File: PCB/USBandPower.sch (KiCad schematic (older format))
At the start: 16 parts

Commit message: WIP
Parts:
- added C?: 22uF, Capacitor_SMD:CP_Elec_10x10.5, symbol Device:CP
- added C?: 0.47uF, Capacitor_SMD:C_0805_2012Metric, symbol Device:C
- added U?: LM2940, Package_TO_SOT_SMD:SOT-223, symbol BritishIdeas:LM2940
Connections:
- net +12V: now also C?.1, U?.1 (IN)
- net GND: now also C?.2, C?.2, U?.2 (GND), U?.4 (GND)
- new net +10V: C?.1, U?.3 (OUT)
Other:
- moved on the sheet: C?, D?, L?, R?, U?

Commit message: WIP.
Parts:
- C?: value 4.7uF 16V e -> 4.7uF; symbol Device:CP -> Device:C
- D?: footprint LED_SMD:LED_PLCC-2 -> LED_SMD:LED_0603_1608Metric
- R?: value 1K -> 620
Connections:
- net +3V3: now also D?.2 (A)
- net +5V: no longer D?.2 (A)
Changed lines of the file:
@@
 $EndComp
 $Comp
-L Device:CP C?
+L Device:C C?
 U 1 1 604917D2
 P 9150 3750
 AR Path="/604917D2" Ref="C?"  Part="1"
 AR Path="/60479334/604917D2" Ref="C?"  Part="1"
-F 0 "C?" H 9250 3750 50  0000 L CNN
-F 1 "4.7uF 16V e" V 9000 3550 50  0000 L CNN
+F 0 "C?" H 8900 3800 50  0000 L CNN
+F 1 "4.7uF" H 8800 3700 50  0000 L CNN
 F 2 "Capacitor_SMD:CP_Elec_4x5.8" H 9188 3600 50  0001 C CNN
 F 3 "~" H 9150 3750 50  0001 C CNN
@@
 F 0 "D?" V 7589 2582 50  0000 R CNN
 F 1 "PWR" V 7498 2582 50  0000 R CNN
-F 2 "LED_SMD:LED_PLCC-2" H 7550 2700 50  0001 C CNN
+F 2 "LED_SMD:LED_0603_1608Metric" H 7550 2700 50  0001 C CNN
 F 3 "~" H 7550 2700 50  0001 C CNN
 	1    7550 2700
@@
 AR Path="/60479334/6045614D" Ref="R?"  Part="1"
 F 0 "R?" V 7343 3250 50  0000 C CNN
-F 1 "1K" V 7434 3250 50  0000 C CNN
+F 1 "620" V 7434 3250 50  0000 C CNN
 F 2 "Resistor_SMD:R_0805_2012Metric" V 7480 3250 50  0001 C CNN
 F 3 "~" H 7550 3250 50  0001 C CNN
 	1    7550 3250
 	-1   0    0    1
-$EndComp
-$Comp
-L power:+5V #PWR?
-U 1 1 60456153
-P 7550 2550
-F 0 "#PWR?" H 7550 2400 50  0001 C CNN
-F 1 "+5V" H 7565 2723 50  0000 C CNN
-F 2 "" H 7550 2550 50  0001 C CNN
-F 3 "" H 7550 2550 50  0001 C CNN
-	1    7550 2550
-	1    0    0    -1
 $EndComp
 $Comp
@@
 	8000 5300 8000 5450
 Connection ~ 8000 5450
+$Comp
+L power:+3V3 #PWR?
+U 1 1 61B0845B
+P 7550 2400
+AR Path="/61B0845B" Ref="#PWR?"  Part="1"
+AR Path="/60479334/61B0845B" Ref="#PWR?"  Part="1"
+F 0 "#PWR?" H 7550 2250 50  0001 C CNN
+F 1 "+3V3" H 7565 2573 50  0000 C CNN
+F 2 "" H 7550 2400 50  0001 C CNN
+F 3 "" H 7550 2400 50  0001 C CNN
+	1    7550 2400
+	1    0    0    -1
+$EndComp
+Wire Wire Line
+	7550 2400 7550 2550
 $EndSCHEMATC

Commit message: WIP
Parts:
- added J?: 12V IN, Britishideas:PhoenixContact_COMBICON_MKDSN_2, symbol Connector:Screw_Terminal_01x02
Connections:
- net +12V: now also J?.2 (Pin_2)
- net GND: now also J?.1 (Pin_1)
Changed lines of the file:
@@
 $Descr A4 11693 8268
 encoding utf-8
-Sheet 2 6
+Sheet 2 3
 Title "MPS Tune-o-Matic"
-Date "2021-12-06"
+Date "2022-02-19"
 Rev "V1.0"
-Comp "(C) andy@britishideas.com 2021"
+Comp "(C) andy@britishideas.com 2022"
 Comment1 "For Bosch D-Jetronic MPS Type 3"
 Comment2 ""
@@
 Wire Wire Line
 	7550 2400 7550 2550
+$Comp
+L power:+12V #PWR?
+U 1 1 62339678
+P 1750 5350
+AR Path="/62339678" Ref="#PWR?"  Part="1"
+AR Path="/60479334/62339678" Ref="#PWR?"  Part="1"
+F 0 "#PWR?" H 1750 5200 50  0001 C CNN
+F 1 "+12V" H 1765 5523 50  0000 C CNN
+F 2 "" H 1750 5350 50  0001 C CNN
+F 3 "" H 1750 5350 50  0001 C CNN
+	1    1750 5350
+	-1   0    0    -1
+$EndComp
+$Comp
+L power:PWR_FLAG #FLG?
+U 1 1 6233967E
+P 1750 5400
+AR Path="/6233967E" Ref="#FLG?"  Part="1"
+AR Path="/60479334/6233967E" Ref="#FLG?"  Part="1"
+F 0 "#FLG?" H 1750 5475 50  0001 C CNN
+F 1 "PWR_FLAG" V 1750 5528 50  0000 L CNN
+F 2 "" H 1750 5400 50  0001 C CNN
+F 3 "~" H 1750 5400 50  0001 C CNN
+	1    1750 5400
+	0    1    -1   0
+$EndComp
+Wire Wire Line
+	1750 5400 1750 5350
+$Comp
+L Connector:Screw_Terminal_01x02 J?
+U 1 1 62339686
+P 1500 5700
+AR Path="/62339686" Ref="J?"  Part="1"
+AR Path="/60479334/62339686" Ref="J?"  Part="1"
+F 0 "J?" H 1580 5692 50  0000 L CNN
+F 1 "12V IN" H 1580 5601 50  0000 L CNN
+F 2 "Britishideas:PhoenixContact_COMBICON_MKDSN_2" H 1500 5700 50  0001 C CNN
+F 3 "~" H 1500 5700 50  0001 C CNN
+F 4 "1729018" H 1500 5700 50  0001 C CNN "manf#"
+	1    1500 5700
+	-1   0    0    1
+$EndComp
+$Comp
+L power:GND #PWR?
+U 1 1 6233968C
+P 1750 5900
+AR Path="/6233968C" Ref="#PWR?"  Part="1"
+AR Path="/60479334/6233968C" Ref="#PWR?"  Part="1"
+F 0 "#PWR?" H 1750 5650 50  0001 C CNN
+F 1 "GND" H 1755 5727 50  0000 C CNN
+F 2 "" H 1750 5900 50  0001 C CNN
+F 3 "" H 1750 5900 50  0001 C CNN
+	1    1750 5900
+	-1   0    0    -1
+$EndComp
+Wire Wire Line
+	1750 5900 1750 5700
+Wire Wire Line
+	1750 5700 1700 5700
+Wire Wire Line
+	1700 5600 1750 5600
+Wire Wire Line
+	1750 5600 1750 5400
+Connection ~ 1750 5400
 $EndSCHEMATC

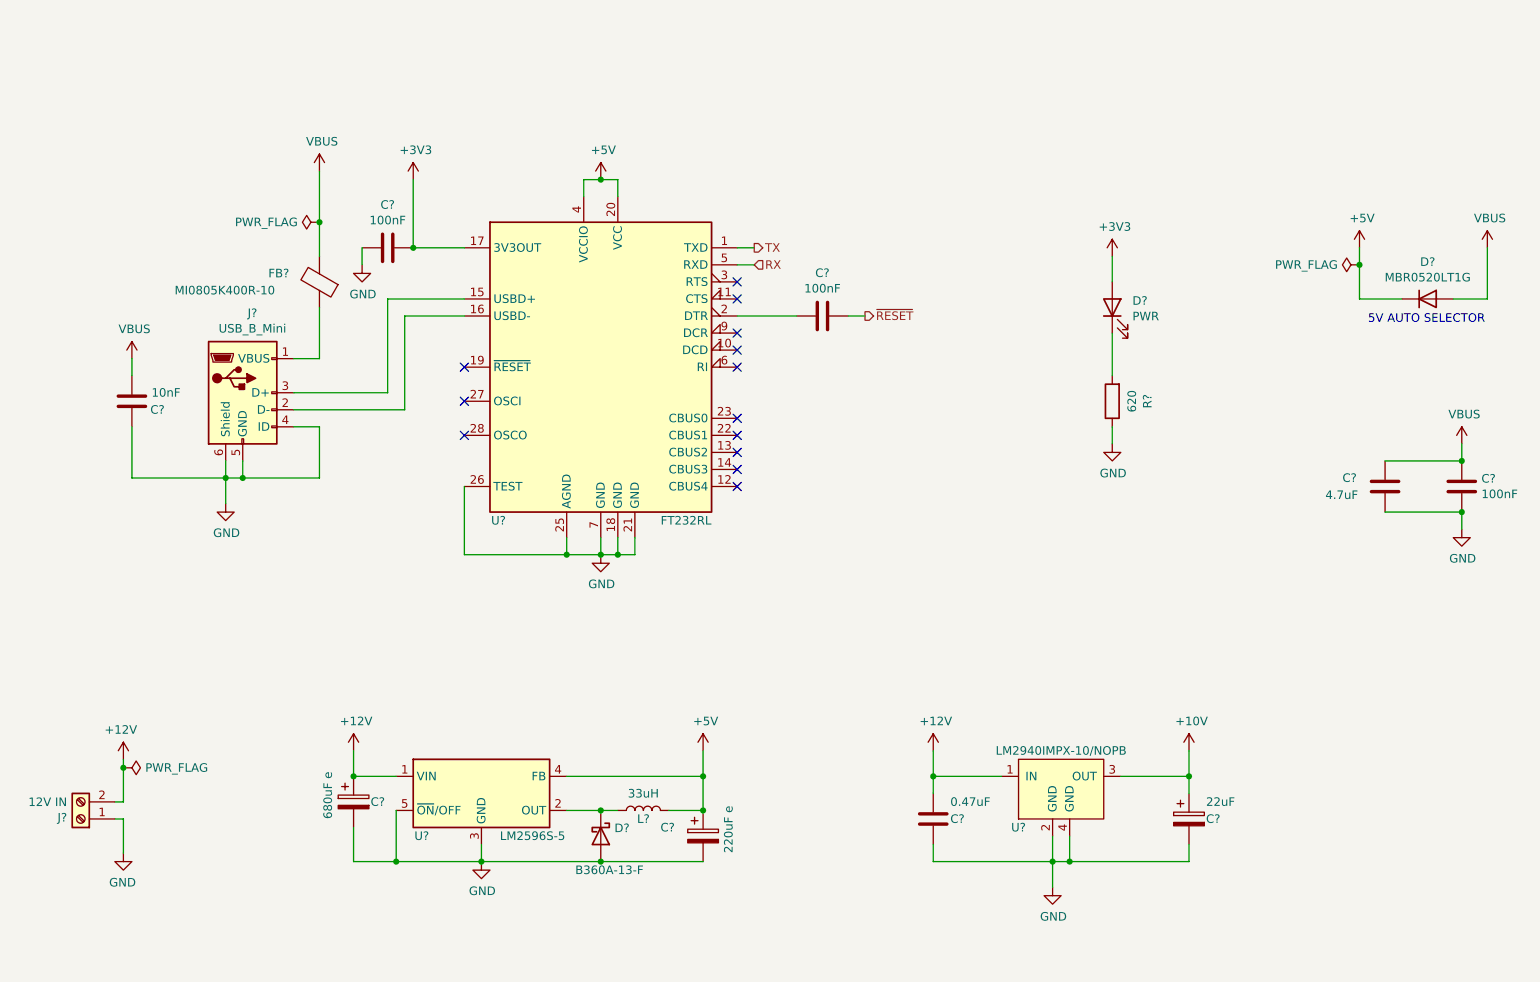
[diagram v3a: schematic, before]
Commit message: Completed schematic. Started work on PCB.
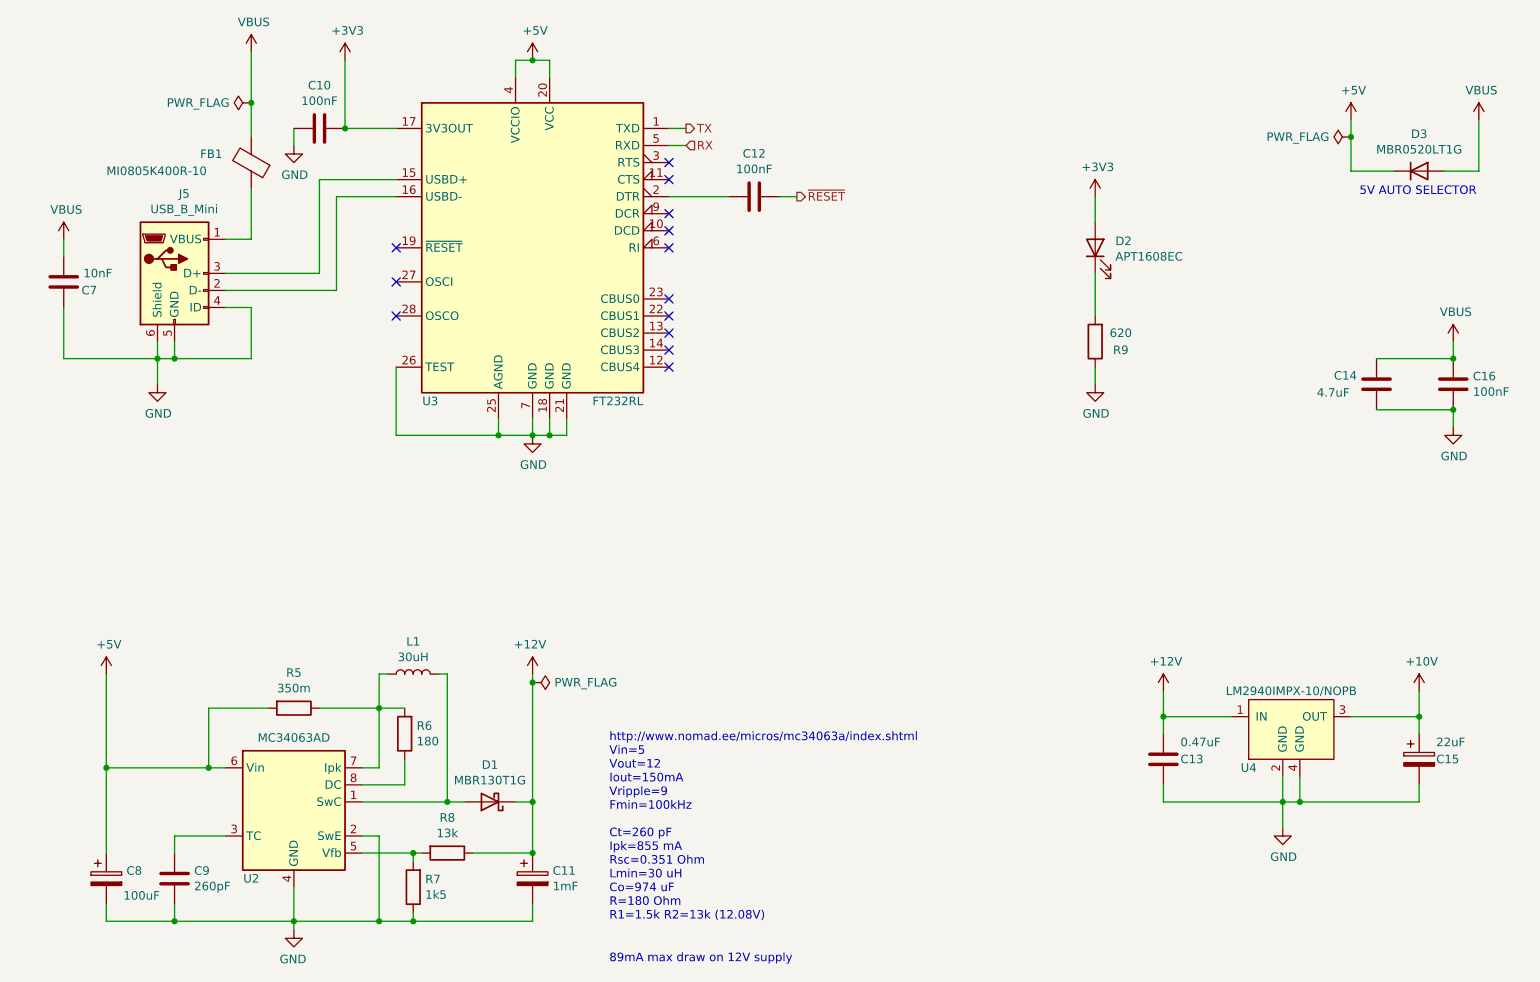
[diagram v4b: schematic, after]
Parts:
- removed C?: 680uF e, Capacitor_SMD:CP_Elec_10x10.5, symbol Device:CP
- removed C?: 220uF e, Capacitor_SMD:CP_Elec_8x6.5, symbol Device:CP
- removed D?: B360A-13-F, Diode_SMD:D_SMA, symbol Device:D_Schottky
- removed J?: 12V IN, Britishideas:PhoenixContact_COMBICON_MKDSN_2, symbol Connector:Screw_Terminal_01x02
- removed L?: 33uH, Britishideas:Wurth-WE-LQS-Inductor, symbol Device:L
- removed U?: LM2596S-5, Package_TO_SOT_SMD:TO-263-5_TabPin3, symbol Regulator_Switching:LM2596S-5
- added C11: 1mF, Capacitor_SMD:CP_Elec_10x10, symbol Device:CP
- added C8: 100uF, Capacitor_SMD:CP_Elec_6.3x5.3, symbol Device:CP
- added C9: 260pF, Capacitor_SMD:C_0603_1608Metric, symbol Device:C
- added D1: MBR130T1G, Britishideas:SOD-123, symbol Device:D_Schottky
- added L1: 30uH, Britishideas:Abracon ASPI-6045S Series Inductors, symbol Device:L
- added R5: 350m, Resistor_SMD:R_2010_5025Metric, symbol Device:R
- added R6: 180, Resistor_SMD:R_0603_1608Metric, symbol Device:R
- added R7: 1k5, Resistor_SMD:R_0603_1608Metric, symbol Device:R
- added R8: 13k, Resistor_SMD:R_0603_1608Metric, symbol Device:R
- added U2: MC34063AD, Package_SO:SOIC-8_3.9x4.9mm_P1.27mm, symbol Regulator_Switching:MC34063AD
- C10, C12, C13, C16, C7: renamed from C?; footprint Capacitor_SMD:C_0805_2012Metric -> Capacitor_SMD:C_0603_1608Metric
- D2: renamed from D?; value PWR -> APT1608EC; manf# (none) -> APT1608EC
- R9: renamed from R?; footprint Resistor_SMD:R_0805_2012Metric -> Resistor_SMD:R_0603_1608Metric
- gave numbers to parts that had none: 7
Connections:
- net +12V: now also C11.1, D1.1 (K), R8.1
- net +5V: now also C8.1, R5.2, U2.6 (Vin)
- net GND: now also C11.2, C8.2, C9.2, R7.1, U2.2 (SwE), U2.4 (GND)
- new net: D1.2 (A), L1.2, U2.1 (SwC)
- new net: C9.1, U2.3 (TC)
- new net: R7.2, R8.2, U2.5 (Vfb)
- new net: L1.1, R5.1, R6.2, U2.7 (Ipk)
- new net: R6.1, U2.8 (DC)
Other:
- note added: "89mA max draw on 12V supply"
- note added: "http://www.nomad.ee/micros/mc34063a/index.shtml\nVin=5\nVout=12\nIout=150mA\nVripple=9\nFmin=100kHz\n\nCt=260 pF\nIpk=855 mA\nRsc=0.351 Ohm\nLmin=30 uH\nCo=974 uF\nR=180 Ohm\nR1=1.5k R2=13k (12.08V)"
- moved on the sheet: C10, C12, C13, C14, C15, C16, C7, D2, D3, FB1, J5, R9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

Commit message: WIP.
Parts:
- C14: footprint Capacitor_SMD:CP_Elec_4x5.8 -> Capacitor_SMD:C_0603_1608Metric
- J5: value USB_B_Mini -> USB_B_Micro; footprint Connector_USB:USB_Mini-B_Wuerth_65100516121_Horizontal -> Connector_USB:USB_Micro-B_Amphenol_10103594-0001LF_Horizontal; symbol Connector:USB_B_Mini -> Connector:USB_B_Micro; manf# 65100516121 -> 10103594-0001LF
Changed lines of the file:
@@
 F 0 "C14" H 8850 3200 50  0000 L CNN
 F 1 "4.7uF" H 8750 3100 50  0000 L CNN
-F 2 "Capacitor_SMD:CP_Elec_4x5.8" H 9138 3000 50  0001 C CNN
+F 2 "Capacitor_SMD:C_0603_1608Metric" H 9138 3000 50  0001 C CNN
 F 3 "~" H 9100 3150 50  0001 C CNN
 	1    9100 3150
@@
 	2750 1650 2750 1750
 $Comp
-L Connector:USB_B_Mini J?
+L Connector:USB_B_Micro J?
 U 1 1 6049775F
 P 2050 2500
@@
 AR Path="/60479334/6049775F" Ref="J5"  Part="1"
 F 0 "J5" H 2107 2967 50  0000 C CNN
-F 1 "USB_B_Mini" H 2107 2876 50  0000 C CNN
-F 2 "Connector_USB:USB_Mini-B_Wuerth_65100516121_Horizontal" H 2200 2450 50  0001 C CNN
+F 1 "USB_B_Micro" H 2107 2876 50  0000 C CNN
+F 2 "Connector_USB:USB_Micro-B_Amphenol_10103594-0001LF_Horizontal" H 2200 2450 50  0001 C CNN
 F 3 "~" H 2200 2450 50  0001 C CNN
-F 4 "65100516121" H 2050 2500 50  0001 C CNN "manf#"
+F 4 "10103594-0001LF" H 2050 2500 50  0001 C CNN "manf#"
 	1    2050 2500
 	1    0    0    -1

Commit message: Added status LED, remove LCD connectors, changed MPS connector to screw terminal block, added 12V power connections, removed 5V to 12V boost converter. Completely reworked PCB. Removed old PCB CAD files.
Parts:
- removed C11: 1mF, Capacitor_SMD:CP_Elec_10x10, symbol Device:CP
- removed C8: 100uF, Capacitor_SMD:CP_Elec_6.3x5.3, symbol Device:CP
- removed C9: 260pF, Capacitor_SMD:C_0603_1608Metric, symbol Device:C
- removed D1: MBR130T1G, Britishideas:SOD-123, symbol Device:D_Schottky
- removed L1: 30uH, Britishideas:Abracon ASPI-6045S Series Inductors, symbol Device:L
- removed R5: 350m, Resistor_SMD:R_2010_5025Metric, symbol Device:R
- removed R6: 180, Resistor_SMD:R_0603_1608Metric, symbol Device:R
- removed R7: 1k5, Resistor_SMD:R_0603_1608Metric, symbol Device:R
- removed R8: 13k, Resistor_SMD:R_0603_1608Metric, symbol Device:R
- removed U2: MC34063AD, Package_SO:SOIC-8_3.9x4.9mm_P1.27mm, symbol Regulator_Switching:MC34063AD
- added J4: 12V 1A IN (5.5/2.5), Connector_BarrelJack:BarrelJack_Wuerth_6941xx301002, symbol Connector:Barrel_Jack_Switch
- added J5: 12V IN, Britishideas:PhoenixContact_COMBICON_MKDSN_2, symbol Connector:Screw_Terminal_01x02
- J3: renamed from J5; symbol Connector:USB_B_Micro -> MPS-Tune-o-Matic-rescue:USB_B_Micro-Connector
- R5: renamed from R9; value 620 -> 150
- U3: renamed from U4; symbol BritishIdeas:LM2940 -> MPS-Tune-o-Matic-rescue:LM2940-BritishIdeas
- renumbered C15 to C10, C12 to C11, C14 to C12, C16 to C13, C10 to C8, C13 to C9, D2 to D1, D3 to D2, U3 to U2
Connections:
- net +12V: now also J4.1, J5.2 (Pin_2)
- net GND: now also J4.2, J4.3, J5.1 (Pin_1)
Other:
- note removed: "89mA max draw on 12V supply"
- note removed: "http://www.nomad.ee/micros/mc34063a/index.shtml\nVin=5\nVout=12\nIout=150mA\nVripple=9\nFmin=100kHz\n\nCt=260 pF\nIpk=855 mA\nRsc=0.351 Ohm\nLmin=30 uH\nCo=974 uF\nR=180 Ohm\nR1=1.5k R2=13k (12.08V)"
- moved on the sheet: C10, C9, U3

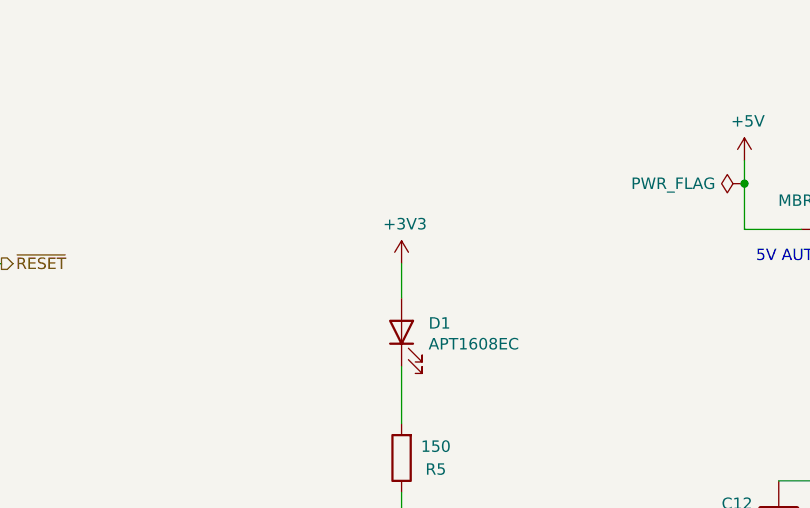
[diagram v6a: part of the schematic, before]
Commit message: Added ground vias. Fixed voltage mistake for power LED.
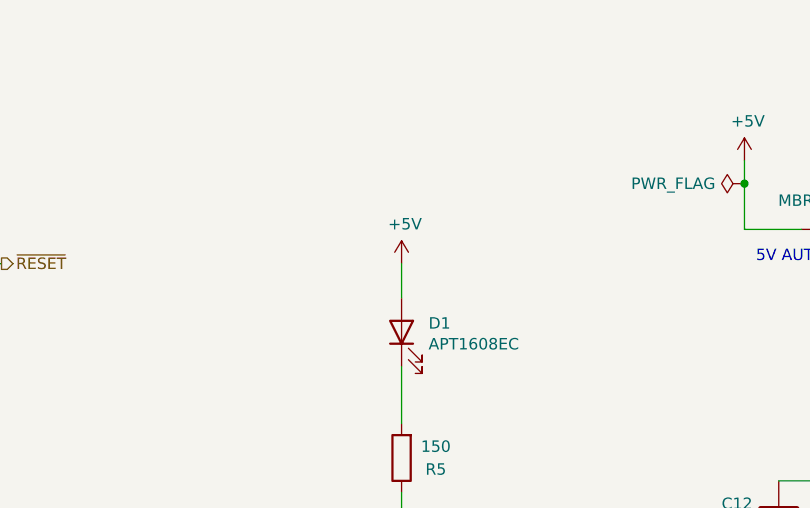
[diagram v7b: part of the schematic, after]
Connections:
- net +3V3: no longer D1.2 (A)
- net +5V: now also D1.2 (A)
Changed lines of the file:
@@
 Sheet 2 3
 Title "MPS Tune-o-Matic"
-Date "2022-10-30"
+Date "2022-10-31"
 Rev "V1.0"
 Comp "(C) andy@britishideas.com 2022"
@@
 $EndComp
 Connection ~ 5350 5650
-$Comp
-L power:+3V3 #PWR?
-U 1 1 61B0845B
-P 7450 2050
-AR Path="/61B0845B" Ref="#PWR?"  Part="1"
-AR Path="/60479334/61B0845B" Ref="#PWR020"  Part="1"
-F 0 "#PWR020" H 7450 1900 50  0001 C CNN
-F 1 "+3V3" H 7465 2223 50  0000 C CNN
-F 2 "" H 7450 2050 50  0001 C CNN
-F 3 "" H 7450 2050 50  0001 C CNN
-	1    7450 2050
-	1    0    0    -1
-$EndComp
 Wire Wire Line
 	7450 2050 7450 2200
@@
 Wire Wire Line
 	3850 5100 3850 5650
+$Comp
+L power:+5V #PWR?
+U 1 1 63607510
+P 7450 2050
+AR Path="/63607510" Ref="#PWR?"  Part="1"
+AR Path="/60479334/63607510" Ref="#PWR020"  Part="1"
+F 0 "#PWR020" H 7450 1900 50  0001 C CNN
+F 1 "+5V" H 7465 2223 50  0000 C CNN
+F 2 "" H 7450 2050 50  0001 C CNN
+F 3 "" H 7450 2050 50  0001 C CNN
+	1    7450 2050
+	1    0    0    -1
+$EndComp
 $EndSCHEMATC

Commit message: Added PCB manufacturing files.
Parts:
- C10: manf# (none) -> MAL214699902E3
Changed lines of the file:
@@
 F 2 "Capacitor_SMD:CP_Elec_10x10.5" H 5388 5750 50  0001 C CNN
 F 3 "~" H 5350 5900 50  0001 C CNN
+F 4 "MAL214699902E3" H 5350 5900 50  0001 C CNN "manf#"
 	1    5350 5900
 	1    0    0    -1
